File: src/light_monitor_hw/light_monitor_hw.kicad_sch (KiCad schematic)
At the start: 0 parts

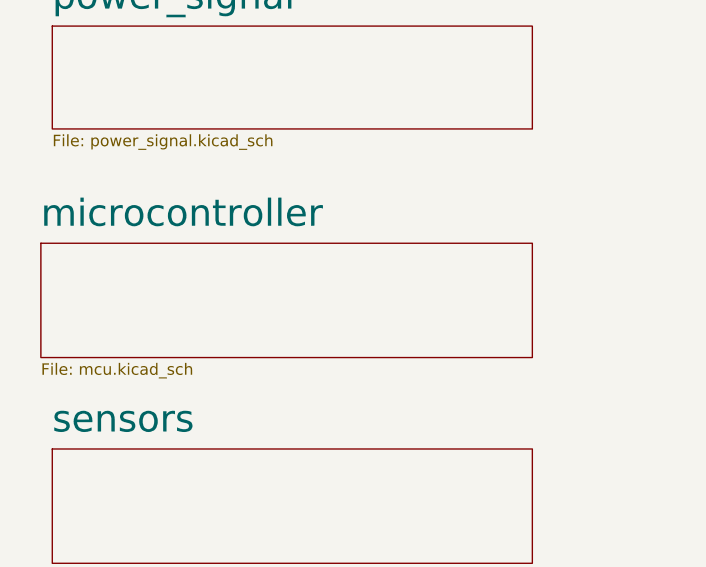
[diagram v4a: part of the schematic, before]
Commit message: [hw][fw] adding reset & boot to mcu, starting power decoupling
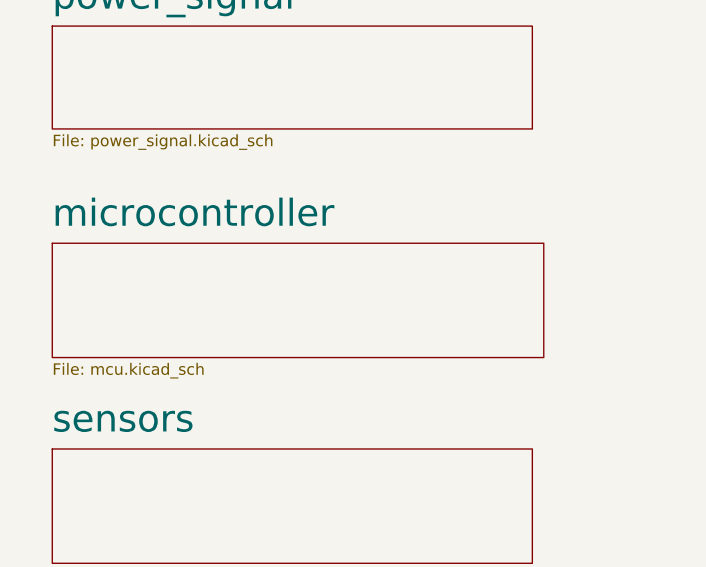
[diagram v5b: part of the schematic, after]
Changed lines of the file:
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@@
     )
   )
-  (sheet (at 20.32 63.5) (size 54.61 12.7) (fields_autoplaced)
+  (sheet (at 21.59 63.5) (size 54.61 12.7) (fields_autoplaced)
     (stroke (width 0.1524) (type solid))
     (fill (color 0 0 0 0.0000))
-    (property "Sheetname" "microcontroller" (at 20.32 61.9234 0)
+    (property "Sheetname" "microcontroller" (at 21.59 61.9234 0)
       (effects (font (size 3 3)) (justify left bottom))
     )
-    (property "Sheetfile" "mcu.kicad_sch" (at 20.32 76.7846 0)
+    (property "Sheetfile" "mcu.kicad_sch" (at 21.59 76.7846 0)
       (effects (font (size 1.27 1.27)) (justify left top))
     )
